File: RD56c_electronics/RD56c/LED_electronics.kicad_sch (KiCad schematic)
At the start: 20 parts, among them IC4 STP24DP05BTR, IC5 STP24DP05BTR, IC6 STP24DP05BTR

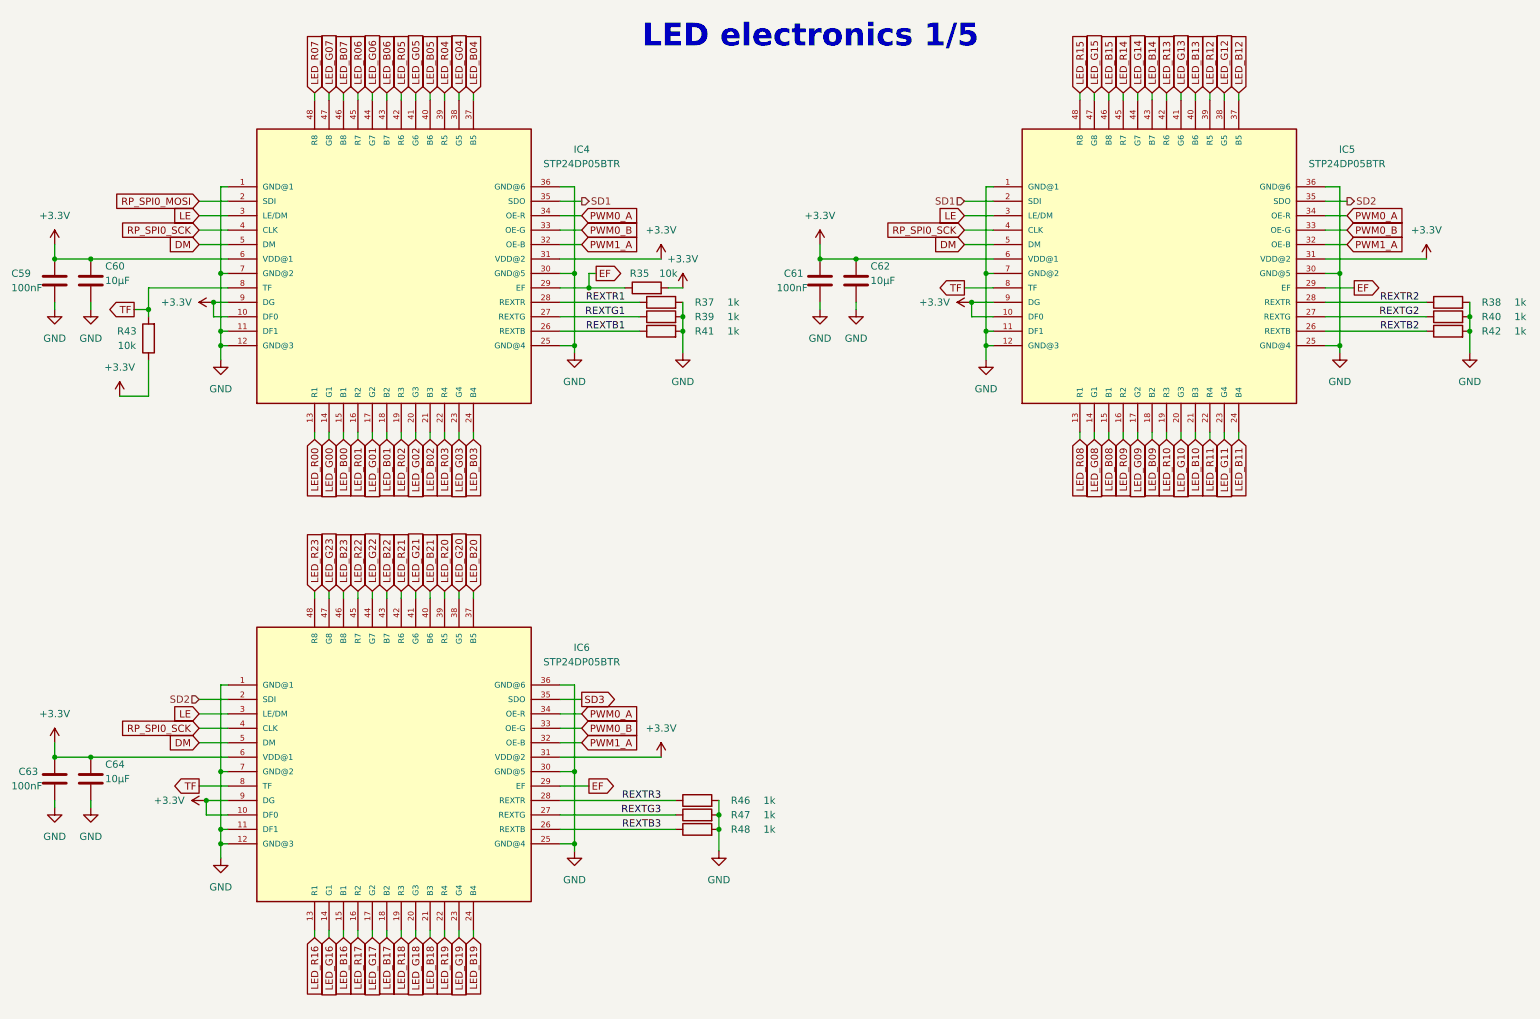
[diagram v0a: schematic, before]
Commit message: added empty_sheet.kicad_wks to KiCAD folders
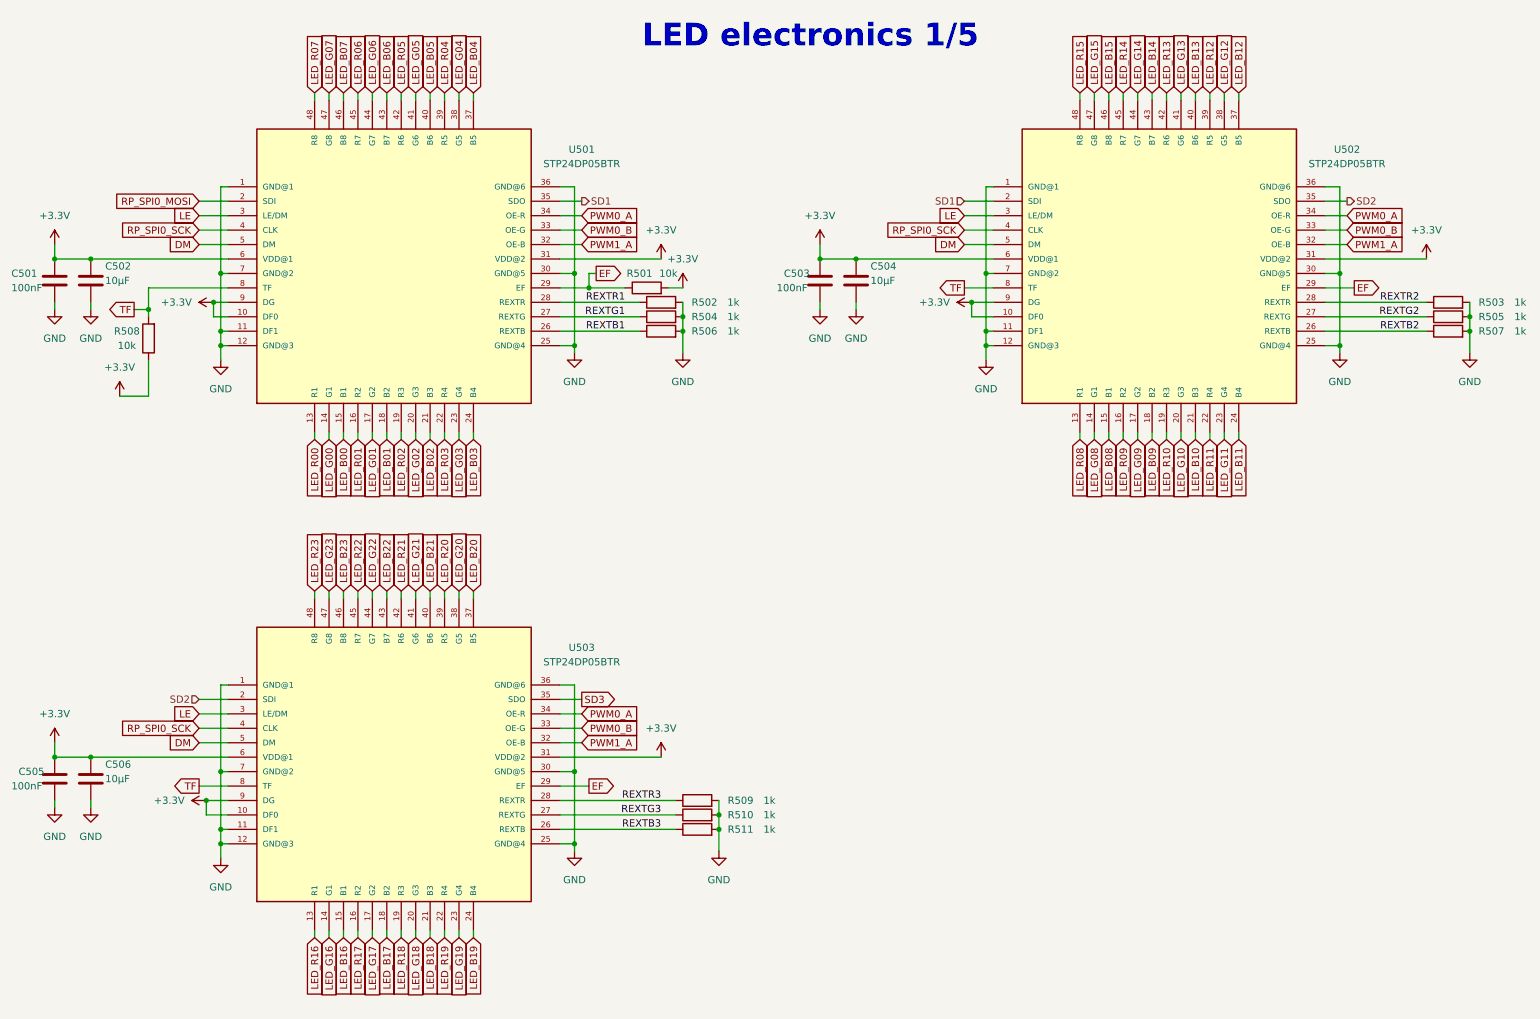
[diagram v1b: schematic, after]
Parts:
- renumbered C59 to C501, C60 to C502, C61 to C503, C62 to C504, C63 to C505, C64 to C506, R35 to R501, R37 to R502, R38 to R503, R39 to R504, R40 to R505, R41 to R506, R42 to R507, R43 to R508, R46 to R509, R47 to R510, R48 to R511, IC4 to U501, IC5 to U502, IC6 to U503
